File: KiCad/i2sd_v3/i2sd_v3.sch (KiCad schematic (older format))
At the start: 55 parts, among them IC1 ATMEGA8-AI, P1 I/O, P10 CD2, P11 CD2, P12 CD1, P13 CD1, P2 COMM_R, P4 CONN_6, P5 CONN_6, P6 CONN_2, P8 FTDI, P9 ISP, SW1 SW_PUSH, U1 MCP1700T-3302E/TT, U2 74HC125, U3 MIC5219-5.0BM5, X1 CRYSTAL

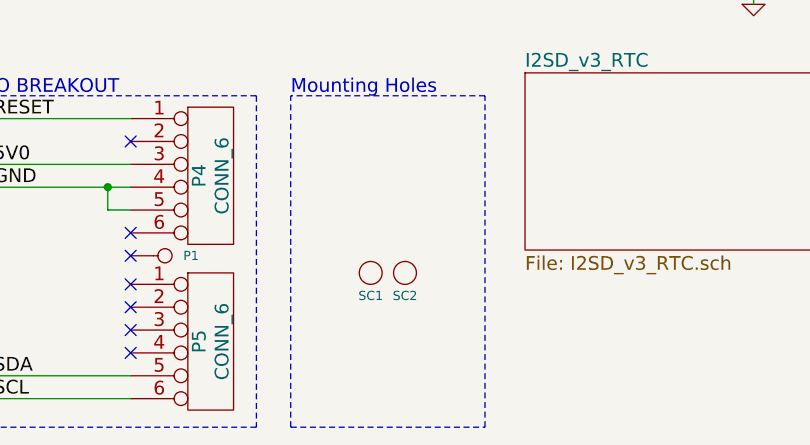
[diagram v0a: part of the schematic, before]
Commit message: i2sd_v3 on 2011 Nov 18 - almost final. smd pads standardized etc
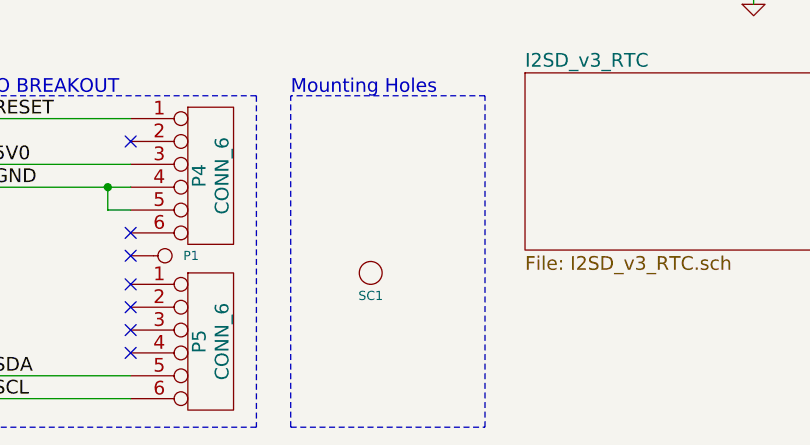
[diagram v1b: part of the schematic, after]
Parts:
- removed SC2: SCREW, vite_3mm, symbol SCREW
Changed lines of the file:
@@
-EESchema Schematic File Version 2  date Tue 15 Nov 2011 10:26:12 PM IST
+EESchema Schematic File Version 2  date 11/18/2011 5:36:14 PM
 LIBS:i2sd_v3
 LIBS:power
@@
 Sheet 1 2
 Title "Buckler, i2sd, v3, with RTC, with HW addressing"
-Date "15 nov 2011"
+Date "18 nov 2011"
 Rev "3"
 Comp "WyoLum"
@@
 	1    0    0    -1
 $EndComp
-$Comp
-L SCREW SC2
-U 1 1 4DCCE754
-P 6500 7075
-F 0 "SC2" H 6500 6975 40  0000 C CNN
-F 1 "SCREW" H 6500 7175 40  0001 C CNN
-F 2 "vite_3mm" H 6500 7075 60  0001 C CNN
-	1    6500 7075
-	1    0    0    -1
-$EndComp

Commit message: i2sd_v3 on 2011 Nov 18 : Added IR receiver
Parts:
- added B18, B19: I/O, I/O, symbol I/O
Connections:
- wire segments 213 -> 218
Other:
- note added: "+5V"
- note added: "DAT"
- note added: "GND"
- note added: "IR SENSOR"
- moved on the sheet: B4
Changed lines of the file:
@@
-EESchema Schematic File Version 2  date 11/18/2011 5:36:14 PM
+EESchema Schematic File Version 2  date 11/18/2011 6:47:08 PM
 LIBS:i2sd_v3
 LIBS:power
@@
 Comment4 ""
 $EndDescr
-NoConn ~ 750  3050
+Wire Notes Line
+	3850 1725 3850 1325
+Wire Notes Line
+	3850 1725 4325 1725
+Wire Notes Line
+	4325 1725 4325 1325
+Wire Notes Line
+	4325 1325 3850 1325
+Connection ~ 4425 800
+Wire Wire Line
+	4425 800  4425 2325
+Wire Wire Line
+	4425 2325 4200 2325
 Wire Wire Line
 	700  3050 550  3050
@@
 	8350 2250 8350 3000
 Wire Wire Line
-	8450 2250 8450 3000
+	8450 3000 8450 2250
 Wire Wire Line
 	7600 975  7600 1850
@@
 Connection ~ 5200 6700
 Wire Wire Line
-	5200 6700 5200 6800
+	5200 6800 5200 6700
 Wire Wire Line
 	5200 6800 5300 6800
@@
 	2900 7000 2000 7000
 Wire Wire Line
-	2700 7300 2700 7200
+	2700 7200 2700 7300
 Connection ~ 10600 3000
 Wire Wire Line
-	10850 3600 10850 3000
+	10850 3000 10850 3600
 Wire Wire Line
 	10850 3600 10575 3600
@@
 	10650 1350 10650 1450
 Wire Wire Line
-	10925 1350 10925 1450
+	10925 1450 10925 1350
 Wire Wire Line
 	10925 1450 8875 1450
@@
 	10400 850  10325 850
 Wire Wire Line
-	10325 1000 10450 1000
+	10450 1000 10325 1000
 Wire Wire Line
 	10450 1000 10450 700
@@
 Connection ~ 5750 1900
 Wire Wire Line
-	5750 1900 6150 1900
+	6150 1900 5750 1900
 Wire Wire Line
 	6150 1900 6150 1950
 Connection ~ 6300 2450
 Wire Wire Line
-	6150 2450 7100 2450
+	7100 2450 6150 2450
 Wire Wire Line
 	6150 2450 6150 2250
@@
 Connection ~ 5750 3100
 Wire Wire Line
-	6150 3100 5750 3100
+	5750 3100 6150 3100
 Connection ~ 6450 4050
 Wire Wire Line
@@
 	5750 1100 5750 4050
 Wire Wire Line
-	5750 4050 7000 4050
+	7000 4050 5750 4050
 Wire Wire Line
 	7000 4050 7000 4650
@@
 	5400 1200 5400 1100
 Wire Wire Line
-	5200 1200 5200 1100
+	5200 1100 5200 1200
 Connection ~ 7600 1100
 Connection ~ 1075 5700
@@
 	1500 2650 975  2650
 Wire Wire Line
-	975  2650 975  800
-Wire Wire Line
-	3400 4350 5400 4350
-Wire Wire Line
-	3400 4250 5200 4250
+	975  800  975  2650
+Wire Wire Line
+	5400 4350 3400 4350
+Wire Wire Line
+	5200 4250 3400 4250
 Connection ~ 8400 3000
 Connection ~ 8025 5700
@@
 	8025 5150 8425 5150
 Wire Wire Line
-	8125 5500 5000 5500
+	5000 5500 8125 5500
 Wire Wire Line
 	2350 800  2350 1950
@@
 	9950 3125 9950 2800
 Wire Wire Line
-	5200 4250 5200 1700
-Wire Wire Line
-	5400 4350 5400 1700
-Wire Wire Line
-	5000 5500 5000 1700
+	5200 1700 5200 4250
+Wire Wire Line
+	5400 1700 5400 4350
+Wire Wire Line
+	5000 1700 5000 5500
 Connection ~ 5000 2650
 Wire Wire Line
@@
 	3400 3150 3625 3150
 Wire Wire Line
-	3400 2550 3625 2550
-Wire Wire Line
 	3400 2450 3625 2450
 Wire Wire Line
@@
 Connection ~ 7100 5700
 Wire Wire Line
-	7100 2450 7100 5700
+	7100 5700 7100 2450
 Connection ~ 7100 3650
 Wire Wire Line
@@
 	1150 6800 800  6800
 Wire Wire Line
-	6150 3450 6150 3650
-Wire Wire Line
-	6150 3650 7100 3650
+	6150 3650 6150 3450
+Wire Wire Line
+	7100 3650 6150 3650
 Connection ~ 6300 3650
 Wire Wire Line
-	6150 2850 6150 3050
-Wire Wire Line
-	6150 3050 7100 3050
+	6150 3050 6150 2850
+Wire Wire Line
+	7100 3050 6150 3050
 Connection ~ 6300 3050
 Wire Wire Line
@@
 	3850 7050 3850 7000
 Wire Wire Line
-	4150 7450 4150 7500
+	4150 7500 4150 7450
 Wire Wire Line
 	4150 7500 3850 7500
@@
 	5200 1100 8625 1100
 Wire Wire Line
-	8625 1100 8625 2300
-Wire Wire Line
-	8625 2300 9400 2300
+	8625 2300 8625 1100
+Wire Wire Line
+	9400 2300 8625 2300
 Wire Wire Line
 	8875 1450 8875 1300
@@
 Connection ~ 8700 800
 Wire Wire Line
-	10600 2025 8700 2025
-Wire Wire Line
-	8700 2025 8700 650
+	8700 2025 10600 2025
+Wire Wire Line
+	8700 650  8700 2025
 Wire Wire Line
 	10450 800  11150 800
@@
 	1400 3150 1500 3150
 Wire Wire Line
-	4375 4050 4500 4050
-Wire Wire Line
-	4500 4050 4500 4725
+	4500 4050 4375 4050
+Wire Wire Line
+	4500 4725 4500 4050
 Wire Notes Line
 	4650 4900 3550 4900
@@
 	7750 1950 7650 1950
 Wire Wire Line
-	7650 1950 7650 3000
-Wire Wire Line
-	7650 3000 10850 3000
+	7650 3000 7650 1950
+Wire Wire Line
+	10850 3000 7650 3000
 Wire Wire Line
 	8500 3000 8500 2250
@@
 	700  2575 700  2550
 Wire Wire Line
-	700  2550 900  2550
-Wire Wire Line
-	900  2550 900  2850
+	900  2550 700  2550
+Wire Wire Line
+	900  2850 900  2550
 Connection ~ 900  2800
 Wire Wire Line
-	550  3050 550  5700
-Wire Wire Line
-	550  5700 8025 5700
+	550  5700 550  3050
+Wire Wire Line
+	8025 5700 550  5700
+Wire Wire Line
+	4000 2100 4000 2550
+Wire Wire Line
+	4000 2550 3400 2550
+Wire Wire Line
+	4200 2325 4200 2100
+Wire Wire Line
+	4100 2250 4100 2100
+Text Notes 4250 1700 1    50   ~ 0
++5V
+Text Notes 4150 1700 1    50   ~ 0
+GND
+Text Notes 4025 1700 1    50   ~ 0
+DAT
+Text Notes 3875 1475 0    50   ~ 0
+IR SENSOR
+$Comp
+L GND #PWR01
+U 1 1 4EC6563E
+P 4100 2250
+F 0 "#PWR01" H 4100 2250 30  0001 C CNN
+F 1 "GND" H 4100 2180 30  0001 C CNN
+	1    4100 2250
+	1    0    0    -1
+$EndComp
+$Comp
+L I/O B19
+U 1 1 4EC65609
+P 4200 1950
+F 0 "B19" H 4280 1950 40  0000 L CNN
+F 1 "I/O" H 4200 2005 30  0001 C CNN
+F 2 "I/O" H 4200 1950 60  0001 C CNN
+	1    4200 1950
+	0    -1   -1   0
+$EndComp
+$Comp
+L I/O B18
+U 1 1 4EC65606
+P 4100 1950
+F 0 "B18" H 4180 1950 40  0000 L CNN
+F 1 "I/O" H 4100 2005 30  0001 C CNN
+F 2 "I/O" H 4100 1950 60  0001 C CNN
+	1    4100 1950
+	0    -1   -1   0
+$EndComp
+NoConn ~ 750  3050
 $Comp
 L C C11
@@
 GND
 $Comp
-L GND #PWR01
+L GND #PWR02
 U 1 1 4E96D558
 P 4500 4725
-F 0 "#PWR01" H 4500 4725 30  0001 C CNN
+F 0 "#PWR02" H 4500 4725 30  0001 C CNN
 F 1 "GND" H 4500 4655 30  0001 C CNN
 	1    4500 4725
@@
 $EndSheet
 $Comp
-L +3.3V #PWR02
+L +3.3V #PWR03
 U 1 1 4E1EF3E1
 P 7600 975
-F 0 "#PWR02" H 7600 935 30  0001 C CNN
+F 0 "#PWR03" H 7600 935 30  0001 C CNN
 F 1 "+3.3V" H 7600 1085 30  0000 C CNN
 	1    7600 975
@@
 $EndComp
 $Comp
-L GND #PWR03
+L GND #PWR04
 U 1 1 4E1EC9C3
 P 9950 1600
-F 0 "#PWR03" H 9950 1600 30  0001 C CNN
+F 0 "#PWR04" H 9950 1600 30  0001 C CNN
 F 1 "GND" H 9950 1530 30  0001 C CNN
 	1    9950 1600
@@
 B_02
 $Comp
-L GND #PWR04
+L GND #PWR05
 U 1 1 4DCFFB44
 P 4000 7550
-F 0 "#PWR04" H 4000 7550 30  0001 C CNN
+F 0 "#PWR05" H 4000 7550 30  0001 C CNN
 F 1 "GND" H 4000 7480 30  0001 C CNN
 	1    4000 7550
@@
 L I/O B4
 U 1 1 4DCD1D41
-P 3775 2550
-F 0 "B4" H 3855 2550 40  0000 L CNN
-F 1 "I/O" H 3775 2605 30  0001 C CNN
-F 2 "I/O" H 3775 2550 60  0001 C CNN
-	1    3775 2550
-	1    0    0    -1
+P 4000 1950
+F 0 "B4" H 4080 1950 40  0000 L CNN
+F 1 "I/O" H 4000 2005 30  0001 C CNN
+F 2 "I/O" H 4000 1950 60  0001 C CNN
+	1    4000 1950
+	0    -1   -1   0
 $EndComp
 $Comp
@@
 GND
 $Comp
-L GND #PWR05
+L GND #PWR06
 U 1 1 4DCAC327
 P 9950 3125
-F 0 "#PWR05" H 9950 3125 30  0001 C CNN
+F 0 "#PWR06" H 9950 3125 30  0001 C CNN
 F 1 "GND" H 9950 3055 30  0001 C CNN
 	1    9950 3125
@@
 $EndComp
 $Comp
-L +5V #PWR06
+L +5V #PWR07
 U 1 1 4D82B1D1
 P 8700 650
-F 0 "#PWR06" H 8700 740 20  0001 C CNN
+F 0 "#PWR07" H 8700 740 20  0001 C CNN
 F 1 "+5V" H 8700 740 30  0000 C CNN
 	1    8700 650
@@
 $EndComp
 $Comp
-L GND #PWR07
+L GND #PWR08
 U 1 1 4D82B1AE
 P 8025 5900
-F 0 "#PWR07" H 8025 5900 30  0001 C CNN
+F 0 "#PWR08" H 8025 5900 30  0001 C CNN
 F 1 "GND" H 8025 5830 30  0001 C CNN
 	1    8025 5900

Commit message: i2sd_v3 : 2011 Nov 22 added INT/SQW 1Hz to PD2 port of ATMega via solder bridge, near Screw/RST Switch
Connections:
- wire segments 218 -> 219

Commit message: i2sd_v3 : Silk screen changes, Box design, connected CD tracks
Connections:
- net labels added: 32k, BAT, RST, SQW
- wire segments 219 -> 223
- no-connect marks 23 -> 15

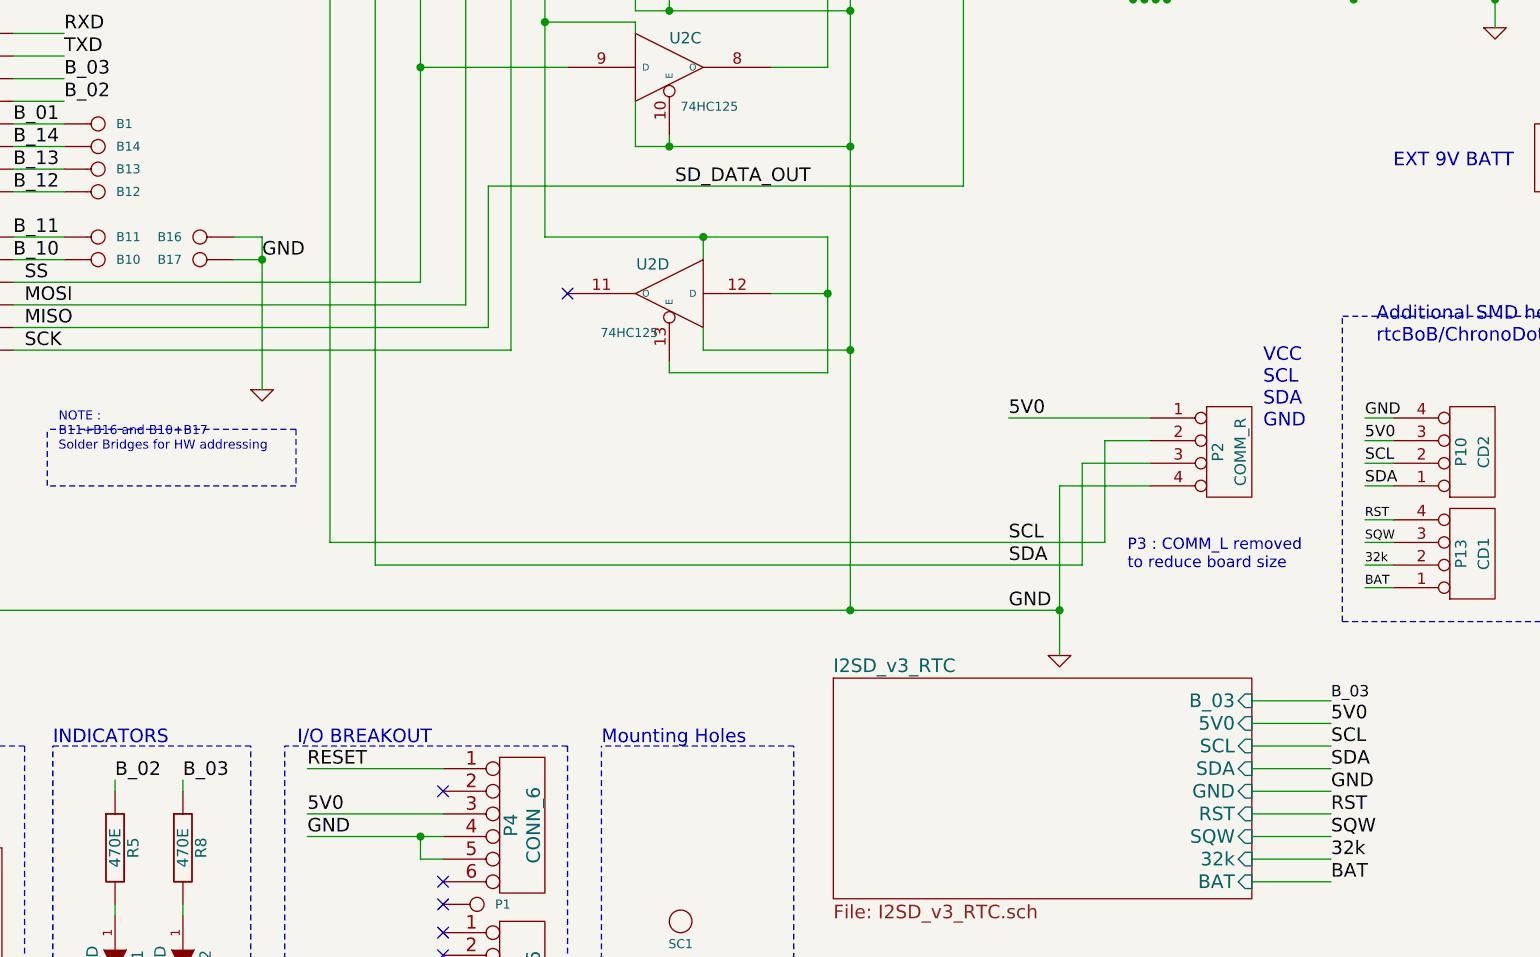
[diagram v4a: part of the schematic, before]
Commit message: i2sd_v3 some minor pcb changes
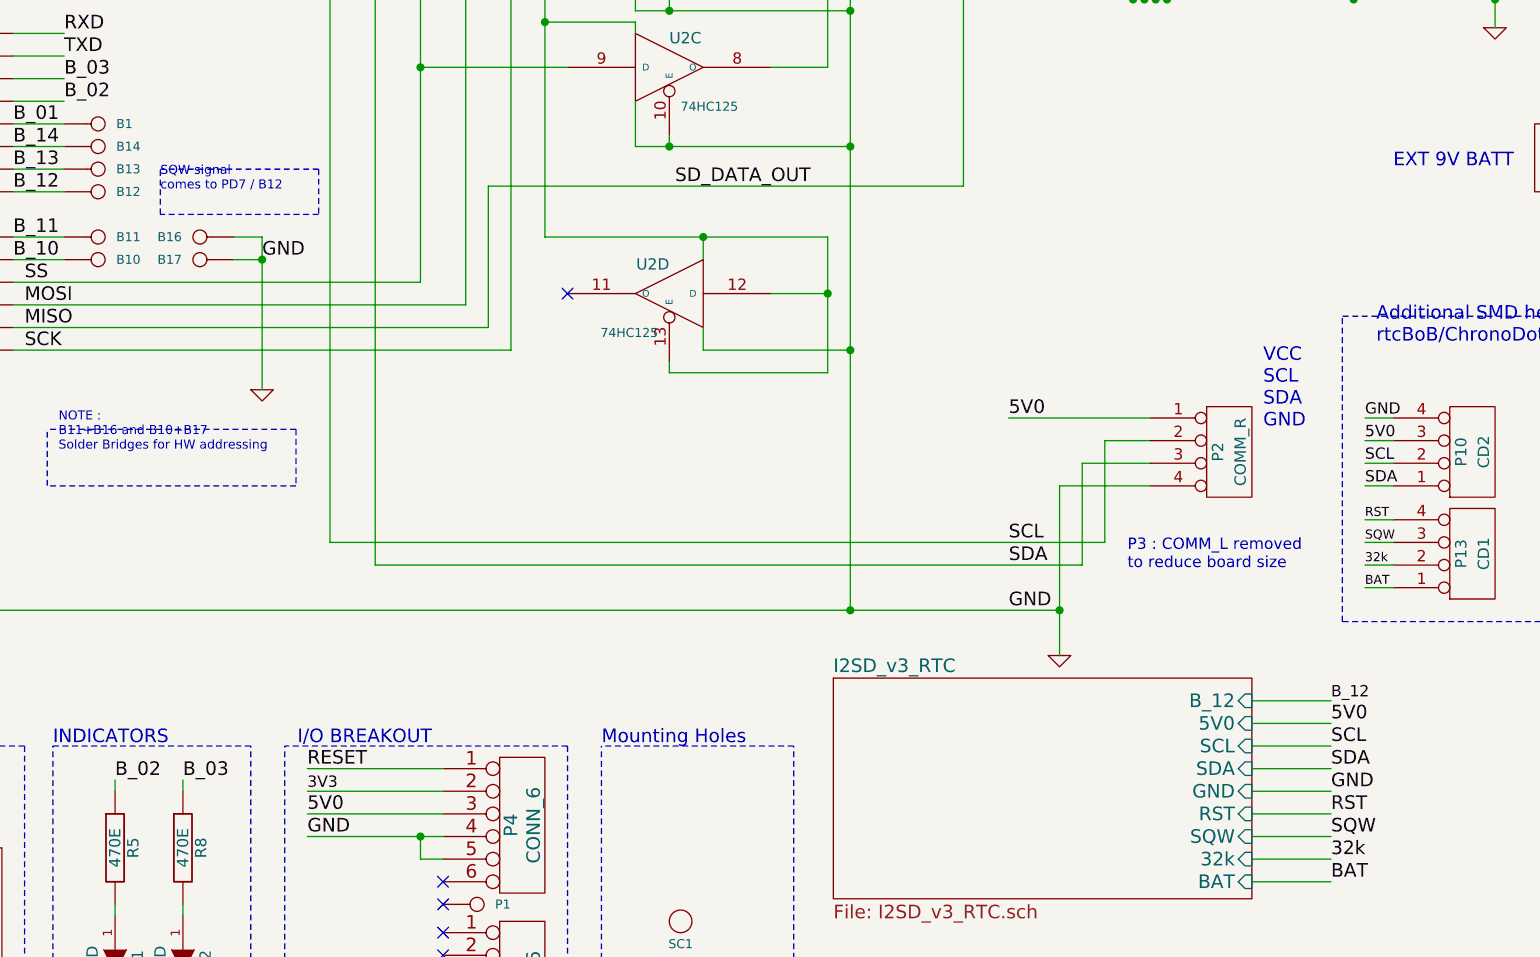
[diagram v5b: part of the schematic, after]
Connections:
- wire segments 223 -> 224
- no-connect marks 15 -> 14
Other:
- note added: "SQW signal\ncomes to PD7 / B12"

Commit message: i2sd_v3 : BootDrive Header added, check it out, Justin
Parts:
- removed X1: CRYSTAL, Xtal_SMD2, symbol CRYSTAL
- added P3: BootDrive, pin_strip_6-90, symbol CONN_6
- added X1: CRYSTAL_2, Xtal_SMD2, symbol CRYSTAL_2
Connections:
- wire segments 224 -> 230
- no-connect marks 14 -> 13
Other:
- note added: "(PD5)"
- note added: "B14 (PD5) : for\nBootDrive Header"
- note added: "BootDrive Header"
- note added: "FTDI Header"
- note added: "ISP/PROG Header"
- note added: "Mounting Hole"
- note removed: "FTDI"
- note removed: "ISP/PROG"
- note removed: "Mounting Holes"
- moved on the sheet: D1, D2, P1, P4, P5, PCB1, R5, R8, SC1
